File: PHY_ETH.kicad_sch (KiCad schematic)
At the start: 1 part, among them U8 LAN8742A

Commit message: lsd circuit in place
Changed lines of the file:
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@@
 			)
 		)
-		(property "Value" "+3V3"
-			(at 26.67 19.05 0)
+		(property "Value" "3V3"
+			(at 29.21 22.8599 0)
 			(effects
 				(font
 					(size 1.27 1.27)
 				)
+				(justify left)
 			)
 		)

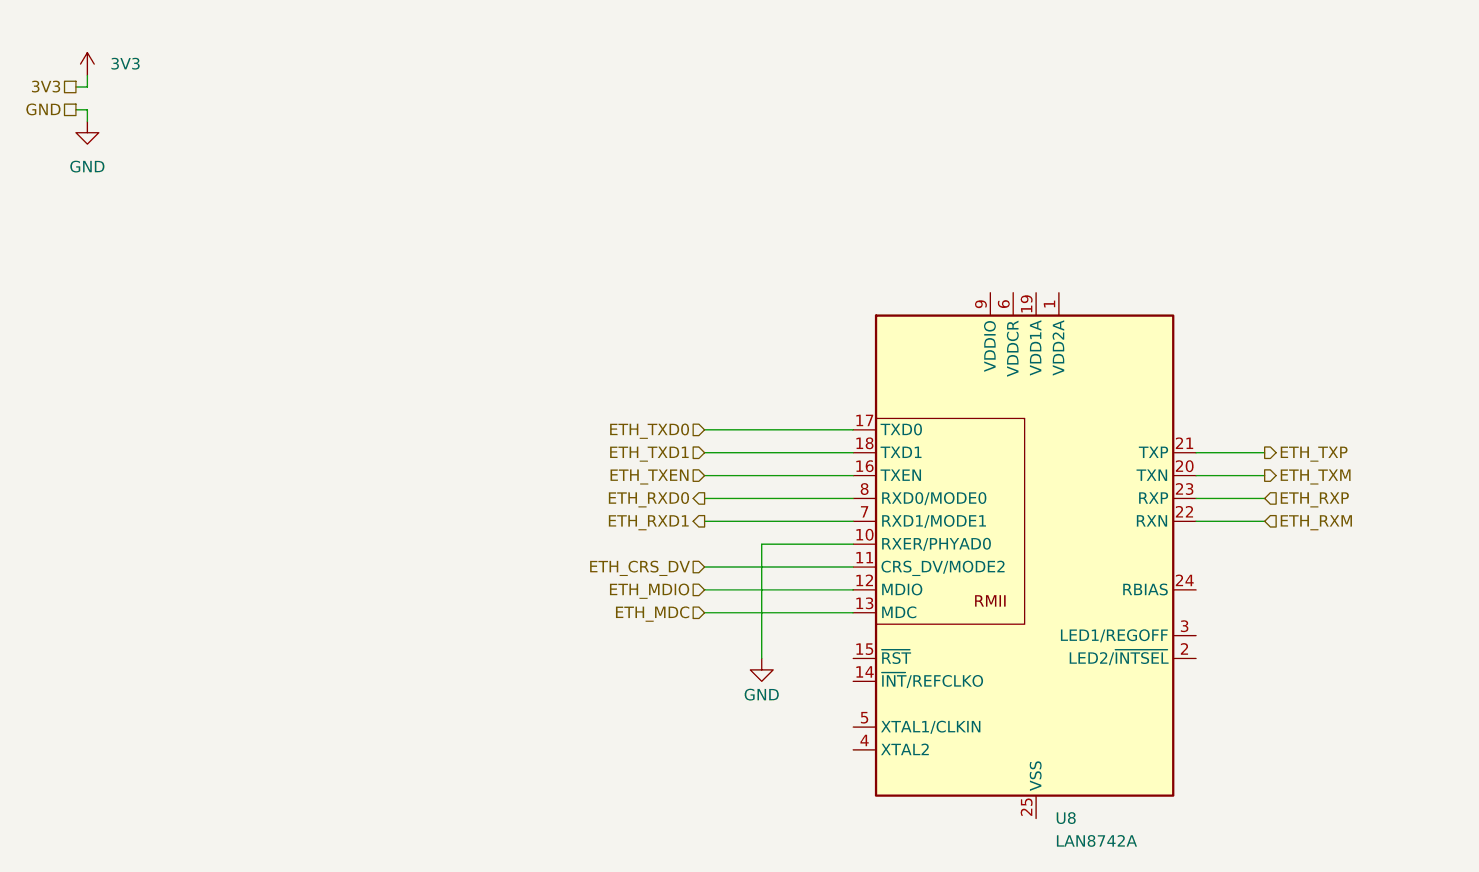
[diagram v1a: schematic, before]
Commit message: added 3.3v gpio input protection
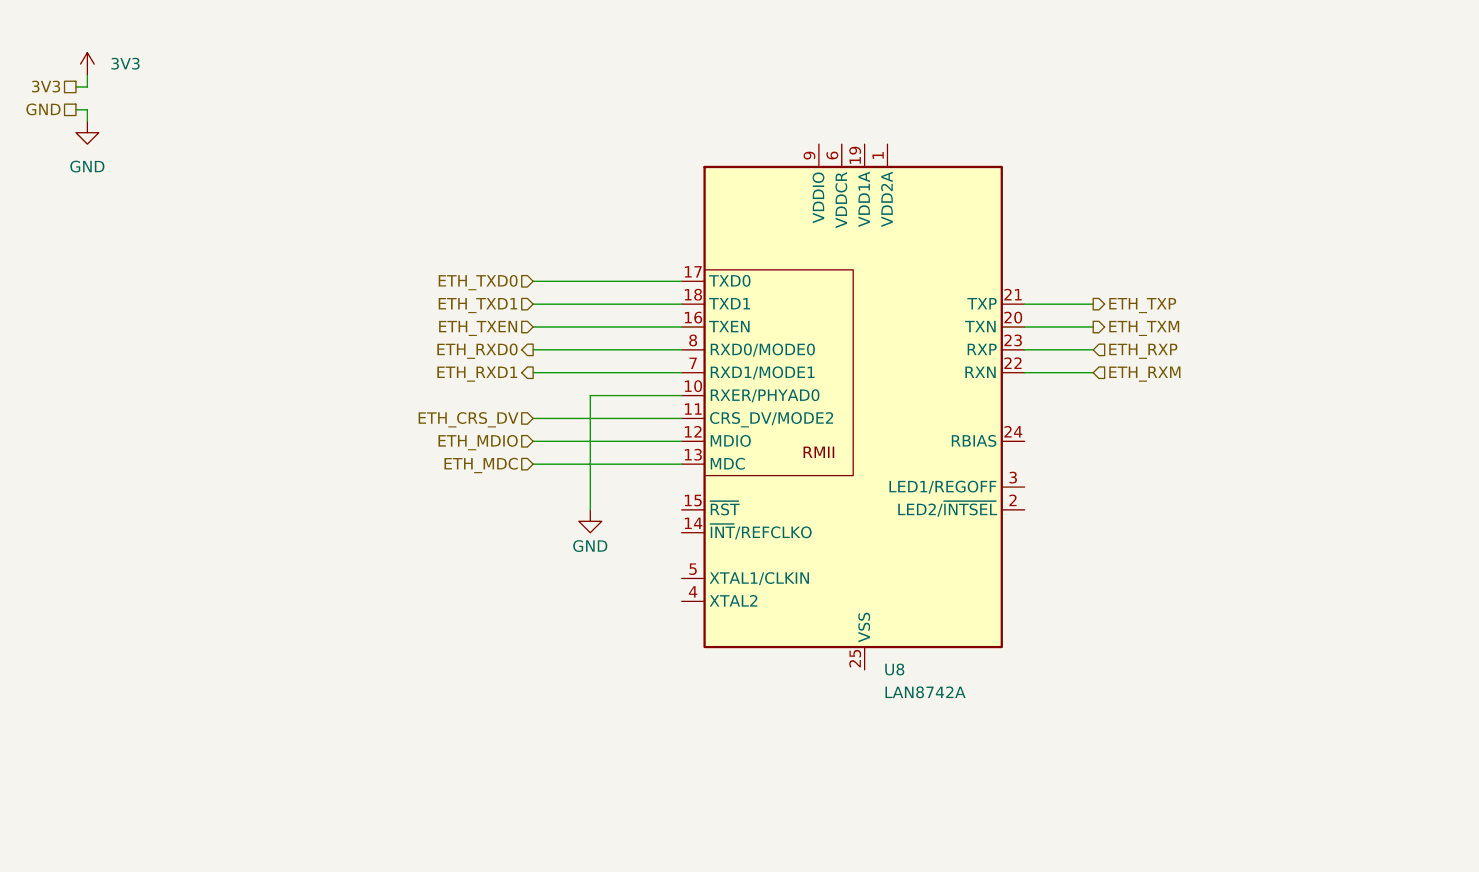
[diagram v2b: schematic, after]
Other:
- moved on the sheet: U8
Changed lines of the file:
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@@
 	(generator "eeschema")
 	(generator_version "9.0")
-	(paper "A4")
-	(wire
-		(pts
-			(xy 95.25 73.66) (xy 111.76 73.66)
-		)
-		(stroke
-			(width 0)
-			(type default)
-		)
-	)
-	(wire
-		(pts
-			(xy 95.25 68.58) (xy 111.76 68.58)
-		)
-		(stroke
-			(width 0)
-			(type default)
-		)
-	)
-	(wire
-		(pts
-			(xy 95.25 78.74) (xy 111.76 78.74)
-		)
-		(stroke
-			(width 0)
-			(type default)
-		)
-	)
-	(wire
-		(pts
-			(xy 95.25 66.04) (xy 111.76 66.04)
-		)
-		(stroke
-			(width 0)
-			(type default)
-		)
-	)
-	(wire
-		(pts
-			(xy 95.25 81.28) (xy 111.76 81.28)
+	(paper "A5")
+	(wire
+		(pts
+			(xy 76.2 57.15) (xy 92.71 57.15)
+		)
+		(stroke
+			(width 0)
+			(type default)
+		)
+	)
+	(wire
+		(pts
+			(xy 76.2 52.07) (xy 92.71 52.07)
+		)
+		(stroke
+			(width 0)
+			(type default)
+		)
+	)
+	(wire
+		(pts
+			(xy 76.2 62.23) (xy 92.71 62.23)
+		)
+		(stroke
+			(width 0)
+			(type default)
+		)
+	)
+	(wire
+		(pts
+			(xy 76.2 49.53) (xy 92.71 49.53)
+		)
+		(stroke
+			(width 0)
+			(type default)
+		)
+	)
+	(wire
+		(pts
+			(xy 76.2 64.77) (xy 92.71 64.77)
 		)
 		(stroke
@@
 	(wire
 		(pts
-			(xy 101.6 76.2) (xy 111.76 76.2)
-		)
-		(stroke
-			(width 0)
-			(type default)
-		)
-	)
-	(wire
-		(pts
-			(xy 95.25 83.82) (xy 111.76 83.82)
+			(xy 82.55 59.69) (xy 92.71 59.69)
+		)
+		(stroke
+			(width 0)
+			(type default)
+		)
+	)
+	(wire
+		(pts
+			(xy 76.2 67.31) (xy 92.71 67.31)
 		)
 		(stroke
@@
 	(wire
 		(pts
-			(xy 149.86 68.58) (xy 157.48 68.58)
+			(xy 130.81 52.07) (xy 138.43 52.07)
 		)
 		(stroke
@@
 	(wire
 		(pts
-			(xy 101.6 88.9) (xy 101.6 76.2)
-		)
-		(stroke
-			(width 0)
-			(type default)
-		)
-	)
-	(wire
-		(pts
-			(xy 149.86 71.12) (xy 157.48 71.12)
-		)
-		(stroke
-			(width 0)
-			(type default)
-		)
-	)
-	(wire
-		(pts
-			(xy 149.86 66.04) (xy 157.48 66.04)
-		)
-		(stroke
-			(width 0)
-			(type default)
-		)
-	)
-	(wire
-		(pts
-			(xy 95.25 71.12) (xy 111.76 71.12)
-		)
-		(stroke
-			(width 0)
-			(type default)
-		)
-	)
-	(wire
-		(pts
-			(xy 95.25 63.5) (xy 111.76 63.5)
-		)
-		(stroke
-			(width 0)
-			(type default)
-		)
-	)
-	(wire
-		(pts
-			(xy 149.86 73.66) (xy 157.48 73.66)
+			(xy 82.55 72.39) (xy 82.55 59.69)
+		)
+		(stroke
+			(width 0)
+			(type default)
+		)
+	)
+	(wire
+		(pts
+			(xy 130.81 54.61) (xy 138.43 54.61)
+		)
+		(stroke
+			(width 0)
+			(type default)
+		)
+	)
+	(wire
+		(pts
+			(xy 130.81 49.53) (xy 138.43 49.53)
+		)
+		(stroke
+			(width 0)
+			(type default)
+		)
+	)
+	(wire
+		(pts
+			(xy 76.2 54.61) (xy 92.71 54.61)
+		)
+		(stroke
+			(width 0)
+			(type default)
+		)
+	)
+	(wire
+		(pts
+			(xy 76.2 46.99) (xy 92.71 46.99)
+		)
+		(stroke
+			(width 0)
+			(type default)
+		)
+	)
+	(wire
+		(pts
+			(xy 130.81 57.15) (xy 138.43 57.15)
 		)
 		(stroke
@@
 	(hierarchical_label "ETH_RXP"
 		(shape input)
-		(at 157.48 71.12 0)
+		(at 138.43 54.61 0)
 		(effects
 			(font
@@
 	(hierarchical_label "ETH_RXM"
 		(shape input)
-		(at 157.48 73.66 0)
+		(at 138.43 57.15 0)
 		(effects
 			(font
@@
 	(hierarchical_label "ETH_TXD1"
 		(shape input)
-		(at 95.25 66.04 180)
+		(at 76.2 49.53 180)
 		(effects
 			(font
@@
 	(hierarchical_label "ETH_TXEN"
 		(shape input)
-		(at 95.25 68.58 180)
+		(at 76.2 52.07 180)
 		(effects
 			(font
@@
 	(hierarchical_label "ETH_RXD0"
 		(shape output)
-		(at 95.25 71.12 180)
+		(at 76.2 54.61 180)
 		(effects
 			(font
@@
 	(hierarchical_label "ETH_CRS_DV"
 		(shape input)
-		(at 95.25 78.74 180)
+		(at 76.2 62.23 180)
 		(effects
 			(font
@@
 	(hierarchical_label "ETH_RXD1"
 		(shape output)
-		(at 95.25 73.66 180)
+		(at 76.2 57.15 180)
 		(effects
 			(font
@@
 	(hierarchical_label "ETH_MDC"
 		(shape input)
-		(at 95.25 83.82 180)
+		(at 76.2 67.31 180)
 		(effects
 			(font
@@
 	(hierarchical_label "ETH_MDIO"
 		(shape input)
-		(at 95.25 81.28 180)
+		(at 76.2 64.77 180)
 		(effects
 			(font
@@
 	(hierarchical_label "ETH_TXP"
 		(shape output)
-		(at 157.48 66.04 0)
+		(at 138.43 49.53 0)
 		(effects
 			(font
@@
 	(hierarchical_label "ETH_TXD0"
 		(shape input)
-		(at 95.25 63.5 180)
+		(at 76.2 46.99 180)
 		(effects
 			(font
@@
 	(hierarchical_label "ETH_TXM"
 		(shape output)
-		(at 157.48 68.58 0)
+		(at 138.43 52.07 0)
 		(effects
 			(font
@@
 	(symbol
 		(lib_id "Interface_Ethernet:LAN8742A")
-		(at 132.08 78.74 0)
+		(at 113.03 62.23 0)
 		(unit 1)
 		(exclude_from_sim no)
@@
 		(fields_autoplaced yes)
 		(property "Reference" "U8"
-			(at 134.2233 106.68 0)
+			(at 115.1733 90.17 0)
 			(effects
 				(font
@@
 		)
 		(property "Value" "LAN8742A"
-			(at 134.2233 109.22 0)
+			(at 115.1733 92.71 0)
 			(effects
 				(font
@@
 		)
 		(property "Footprint" "Package_DFN_QFN:VQFN-24-1EP_4x4mm_P0.5mm_EP2.5x2.5mm_ThermalVias"
-			(at 133.35 105.41 0)
+			(at 114.3 88.9 0)
 			(effects
 				(font
@@
 		)
 		(property "Datasheet" "http://ww1.microchip.com/downloads/en/DeviceDoc/8742a.pdf"
-			(at 132.08 118.11 0)
+			(at 113.03 101.6 0)
 			(effects
 				(font
@@
 		)
 		(property "Description" "LAN8720 Ethernet PHY with RMII interface, QFN-24"
-			(at 132.08 78.74 0)
+			(at 113.03 62.23 0)
 			(effects
 				(font
@@
 	(symbol
 		(lib_id "power:GND")
-		(at 101.6 88.9 0)
+		(at 82.55 72.39 0)
 		(unit 1)
 		(exclude_from_sim no)
@@
 		(dnp no)
 		(property "Reference" "#PWR047"
-			(at 101.6 95.25 0)
+			(at 82.55 78.74 0)
 			(effects
 				(font
@@
 		)
 		(property "Value" "GND"
-			(at 101.6 92.964 0)
+			(at 82.55 76.454 0)
 			(effects
 				(font
@@
 		)
 		(property "Footprint" ""
-			(at 101.6 88.9 0)
+			(at 82.55 72.39 0)
 			(effects
 				(font
@@
 		)
 		(property "Datasheet" ""
-			(at 101.6 88.9 0)
+			(at 82.55 72.39 0)
 			(effects
 				(font
@@
 		)
 		(property "Description" "Power symbol creates a global label with name \"GND\" , ground"
-			(at 101.6 88.9 0)
-			(effects
-				(font
+			(at 82.55 72.39 0)
+			(effects
+				(font

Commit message: updated CAN
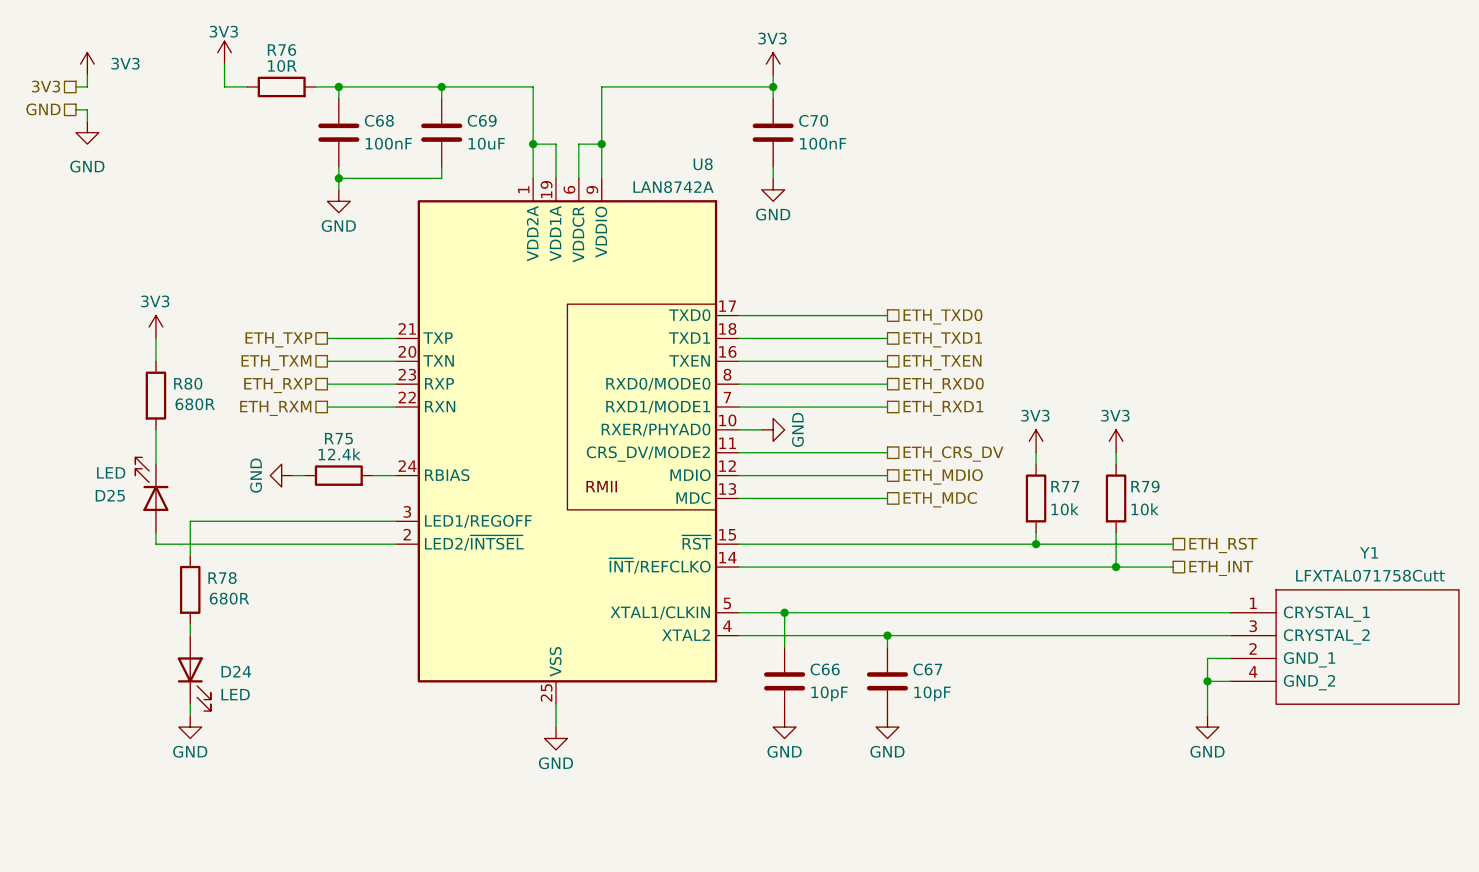
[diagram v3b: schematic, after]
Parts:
- added C66: 10pF, Capacitor_SMD:C_0603_1608Metric_Pad1.08x0.95mm_HandSolder, symbol Device:C
- added C67: 10pF, symbol Device:C
- added C68, C70: 100nF, Capacitor_SMD:C_0603_1608Metric_Pad1.08x0.95mm_HandSolder, symbol Device:C
- added C69: 10uF, Capacitor_SMD:C_0603_1608Metric_Pad1.08x0.95mm_HandSolder, symbol Device:C
- added D24, D25: LED, LED_SMD:LED_0603_1608Metric_Pad1.05x0.95mm_HandSolder, symbol Device:LED
- added R75: 12.4k, Resistor_SMD:R_0603_1608Metric_Pad0.98x0.95mm_HandSolder, symbol Device:R
- added R76: 10R, Resistor_SMD:R_0603_1608Metric_Pad0.98x0.95mm_HandSolder, symbol Device:R
- added R77, R79: 10k, Resistor_SMD:R_0603_1608Metric_Pad0.98x0.95mm_HandSolder, symbol Device:R
- added R78, R80: 680R, Resistor_SMD:R_0603_1608Metric_Pad0.98x0.95mm_HandSolder, symbol Device:R
- added Y1: LFXTAL071758Cutt, LFXTAL071758Cutt, symbol 0_SamacSys_Parts:LFXTAL071758Cutt
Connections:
- net 3V3: now also U8.6 (VDDCR), U8.9 (VDDIO), C70.1, R76.1, R77.1, R79.1, R80.1
- net GND: now also U8.25 (VSS), C66.2, C67.2, C68.2, C69.2, C70.2, D24.1 (K), R75.1, Y1.2 (GND_1), Y1.4 (GND_2)
- net at U8.1 (VDD2A): now also U8.19 (VDD1A), C68.1, C69.1, R76.2
- net ETH_INT: now reaches U8.14 (~{INT}/REFCLKO)
- net ETH_INT: now also R79.2
- net ETH_RST: now reaches U8.15 (~{RST})
- net ETH_RST: now also R77.2
- net at U8.2 (LED2/~{INTSEL}): now also D25.2 (A)
- net at U8.24 (RBIAS): now also R75.2
- net at U8.3 (LED1/REGOFF): now also R78.1
- net at U8.4 (XTAL2): now also C67.1, Y1.3 (CRYSTAL_2)
- net at U8.5 (XTAL1/CLKIN): now also C66.1, Y1.1 (CRYSTAL_1)
- new net: D25.1 (K), R80.2
- new net: D24.2 (A), R78.2
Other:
- moved on the sheet: U8

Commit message: finished initial esp routing
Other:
- moved on the sheet: D24, R78
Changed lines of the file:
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@@
 	(wire
 		(pts
-			(xy 38.1 93.98) (xy 38.1 95.25)
+			(xy 50.8 93.98) (xy 50.8 95.25)
 		)
 		(stroke
@@
 	(wire
 		(pts
-			(xy 38.1 73.66) (xy 60.96 73.66)
-		)
-		(stroke
-			(width 0)
-			(type default)
-		)
-	)
-	(wire
-		(pts
-			(xy 38.1 85.09) (xy 38.1 86.36)
+			(xy 50.8 73.66) (xy 60.96 73.66)
+		)
+		(stroke
+			(width 0)
+			(type default)
+		)
+	)
+	(wire
+		(pts
+			(xy 50.8 85.09) (xy 50.8 86.36)
 		)
 		(stroke
@@
 	(wire
 		(pts
-			(xy 38.1 73.66) (xy 38.1 77.47)
+			(xy 50.8 73.66) (xy 50.8 77.47)
 		)
 		(stroke
@@
 	(symbol
 		(lib_id "Device:LED")
-		(at 38.1 90.17 90)
+		(at 50.8 90.17 90)
 		(unit 1)
 		(exclude_from_sim no)
@@
 		(dnp no)
 		(property "Reference" "D24"
-			(at 41.402 90.424 90)
+			(at 54.102 90.424 90)
 			(effects
 				(font
@@
 		)
 		(property "Value" "LED"
-			(at 41.402 92.964 90)
+			(at 54.102 92.964 90)
 			(effects
 				(font
@@
 		)
 		(property "Footprint" "LED_SMD:LED_0603_1608Metric_Pad1.05x0.95mm_HandSolder"
-			(at 38.1 90.17 0)
+			(at 50.8 90.17 0)
 			(effects
 				(font
@@
 		)
 		(property "Datasheet" "~"
-			(at 38.1 90.17 0)
+			(at 50.8 90.17 0)
 			(effects
 				(font
@@
 		)
 		(property "Description" "Light emitting diode"
-			(at 38.1 90.17 0)
+			(at 50.8 90.17 0)
 			(effects
 				(font
@@
 		)
 		(property "Sim.Pins" "1=K 2=A"
-			(at 38.1 90.17 0)
+			(at 50.8 90.17 0)
 			(effects
 				(font
@@
 	(symbol
 		(lib_id "Device:R")
-		(at 38.1 81.28 0)
+		(at 50.8 81.28 0)
 		(unit 1)
 		(exclude_from_sim no)
@@
 		(dnp no)
 		(property "Reference" "R78"
-			(at 41.656 80.01 0)
+			(at 54.356 80.01 0)
 			(effects
 				(font
@@
 		)
 		(property "Value" "680R"
-			(at 42.418 82.296 0)
+			(at 55.118 82.296 0)
 			(effects
 				(font
@@
 		)
 		(property "Footprint" "Resistor_SMD:R_0603_1608Metric_Pad0.98x0.95mm_HandSolder"
-			(at 36.322 81.28 90)
+			(at 49.022 81.28 90)
 			(effects
 				(font
@@
 		)
 		(property "Datasheet" "~"
-			(at 38.1 81.28 0)
+			(at 50.8 81.28 0)
 			(effects
 				(font
@@
 		)
 		(property "Description" "Resistor"
-			(at 38.1 81.28 0)
+			(at 50.8 81.28 0)
 			(effects
 				(font
@@
 	(symbol
 		(lib_id "power:GND")
-		(at 38.1 95.25 0)
+		(at 50.8 95.25 0)
 		(unit 1)
 		(exclude_from_sim no)
@@
 		(dnp no)
 		(property "Reference" "#PWR0243"
-			(at 38.1 101.6 0)
+			(at 50.8 101.6 0)
 			(effects
 				(font
@@
 		)
 		(property "Value" "GND"
-			(at 38.1 99.314 0)
+			(at 50.8 99.314 0)
 			(effects
 				(font
@@
 		)
 		(property "Footprint" ""
-			(at 38.1 95.25 0)
+			(at 50.8 95.25 0)
 			(effects
 				(font
@@
 		)
 		(property "Datasheet" ""
-			(at 38.1 95.25 0)
+			(at 50.8 95.25 0)
 			(effects
 				(font
@@
 		)
 		(property "Description" "Power symbol creates a global label with name \"GND\" , ground"
-			(at 38.1 95.25 0)
-			(effects
-				(font
+			(at 50.8 95.25 0)
+			(effects
+				(font
